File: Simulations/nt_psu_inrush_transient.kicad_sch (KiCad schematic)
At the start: 10 parts

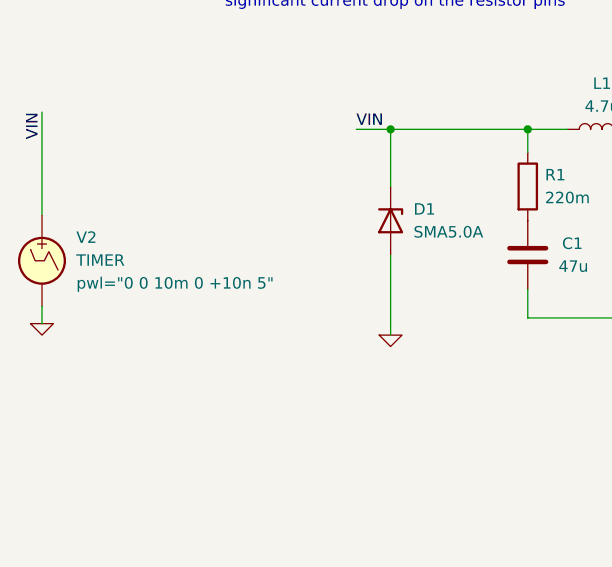
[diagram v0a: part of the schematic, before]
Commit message: switch power to 9V
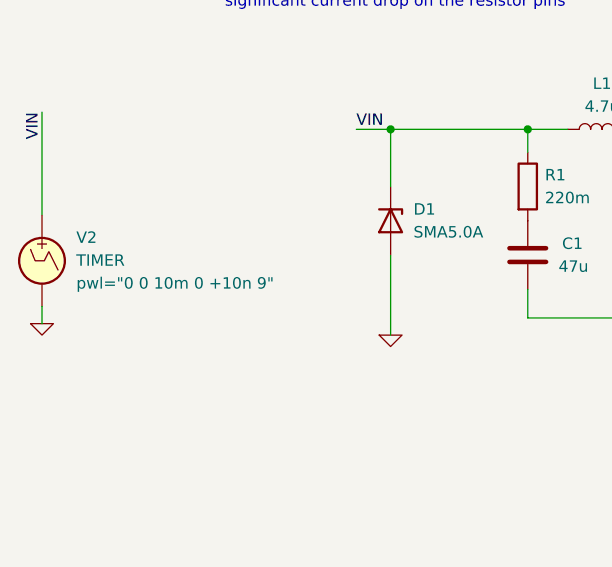
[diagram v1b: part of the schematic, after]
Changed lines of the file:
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@@
       (effects (font (size 1.27 1.27)) (justify left) hide)
     )
-    (property "Sim.Params" "pwl=\"0 0 10m 0 +10n 5\"" (at 90.17 99.0242 0)
+    (property "Sim.Params" "pwl=\"0 0 10m 0 +10n 9\"" (at 90.17 99.0242 0)
       (effects (font (size 1.27 1.27)) (justify right))
     )

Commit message: fine tuning before layout
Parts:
- removed C3: 2u, symbol Device:C
- removed D1: SMA5.0A, symbol Device:D_Zener
- removed R4: 1k, symbol Device:R
- R1, R2: value 220m -> 100m
- R3: value 250 -> 50
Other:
- note added: ".tran 1u 40m"
- note removed: ".tran 1u 200m"
- moved on the sheet: V2
